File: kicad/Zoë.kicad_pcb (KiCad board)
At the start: 4 copper layers, 55 x 35 mm, 43 parts, among them X2Y-CAN 4.7nF X2Y, X2Y-RS485 4.7nF X2Y

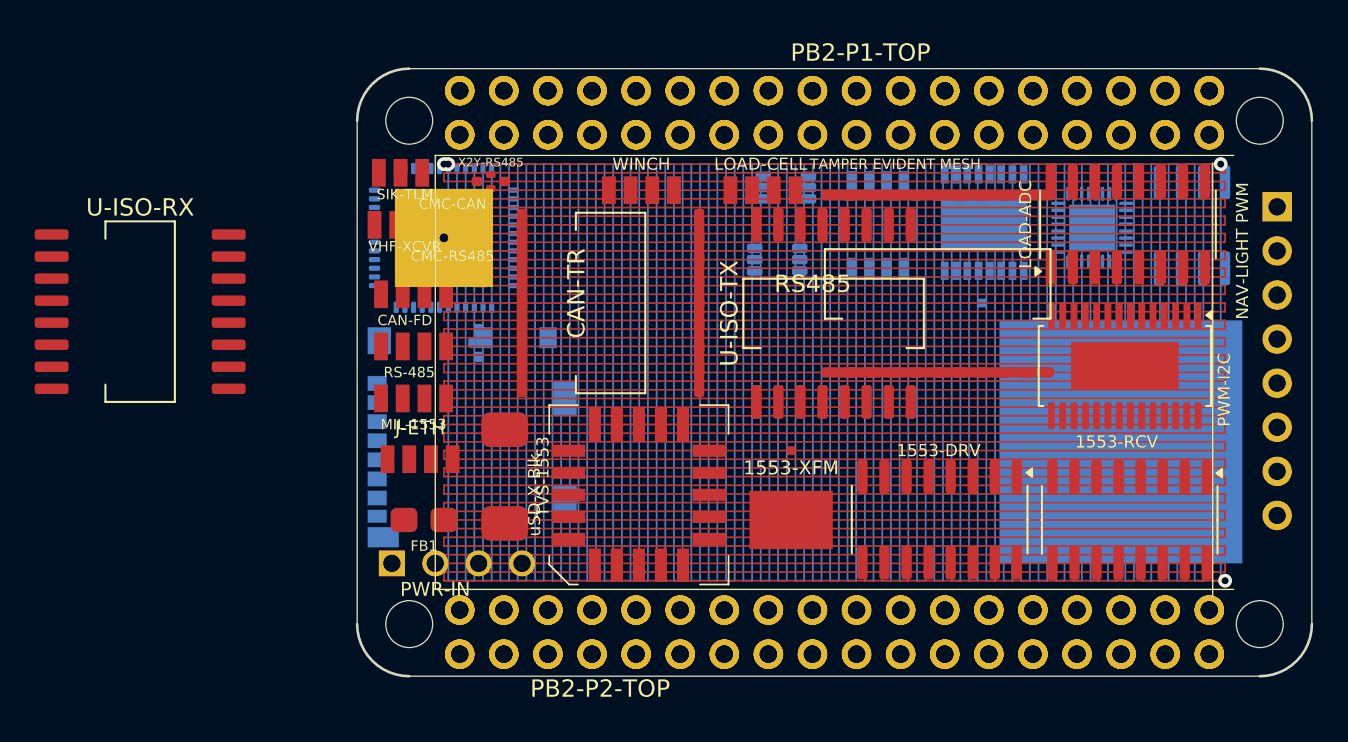
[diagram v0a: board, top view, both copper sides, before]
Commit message: updated zoe and emma boards.  renamed all xcvr files to emma.  updated project index to reflect the name change.
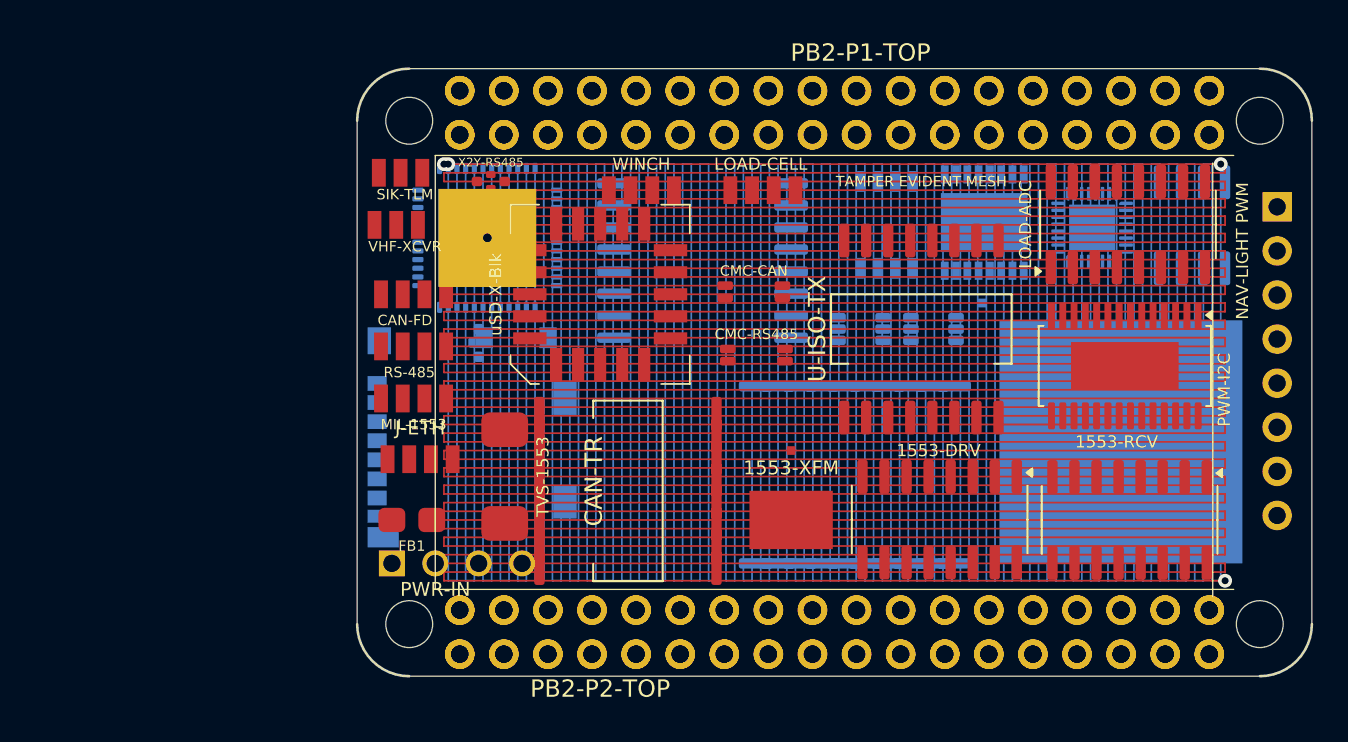
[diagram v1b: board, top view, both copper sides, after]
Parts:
- RS485, U-ISO-RX: moved to B.Cu
- moved U-ISO-RX 32.5 mm to (140.9, 98.6), turned to 180 degrees
- moved CMC-RS485 18.1 mm to (144.0, 104.0)
- moved CMC-CAN 17.8 mm to (143.8, 100.3)
- moved RS485 12.0 mm to (149.7, 110.9)
- moved TVS-CAN 11.8 mm to (154.2, 102.5)
- moved uSD-X-Blk 11.8 mm to (135.0, 100.5)
- moved CAN-TR 10.9 mm to (136.6, 111.8)
- moved TVS-RS485 6.25 mm to (150.0, 102.5)
- moved U-ISO-TX 5.13 mm to (153.5, 102.5)
- moved ETH-PHY 2.50 mm to (128.5, 97.2)
- moved FB1 0.70 mm to (124.2, 113.5)
- moved T-ETH1 0.50 mm to (151.5, 96.5)
- renumbered T-ETH to T-ETH1
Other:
- board text added: "Resillient Communications Cape For the PocketBeagle2 CC BY 4.0 — May 2026 Steve Griffing PE(CSE), CISSP-ISSEP, CPP Griffing Technology LLC github.com/Stab-Rabbit-Coding"
- board text removed: "UAV Resillient Communications Cape For the PocketBeagle2 CC BY 4.0 — May 2026 Steve Griffing, PE(CSE), CISSP-ISSEP, CPP Griffing Technology LLC www.github.com/Stab-Rabbit-Coding"
